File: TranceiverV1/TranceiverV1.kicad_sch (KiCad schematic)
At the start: 21 parts, among them J1 Conn_01x03_Socket, J3 Battery, J4 Conn_01x03_Pin, M1 Motor_Servo, SW1 SW_Push_Open, U1 NRF24L01_, U3 102010388, U4 LD1086DTTR

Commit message: changed switch
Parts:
- removed SW1: SW_Push_Open, Button_Switch_THT:SW_PUSH_1P1T_6x3.5mm_H5.0_APEM_MJTP1250, symbol Switch:SW_Push_Open
- added S3: ATE1D-2M3-10-Z, ATE1D-2M3-10-Z:SW_ATE1D-2M3-10-Z, symbol ATE1D-2M3-10-Z:ATE1D-2M3-10-Z
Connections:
- net GND: now also S3.3
- net Regulator_In: now also S3.1
- net at J3.1 (Pin_1): now also S3.2
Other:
- note added: "SW_SPST"
- moved on the sheet: J3

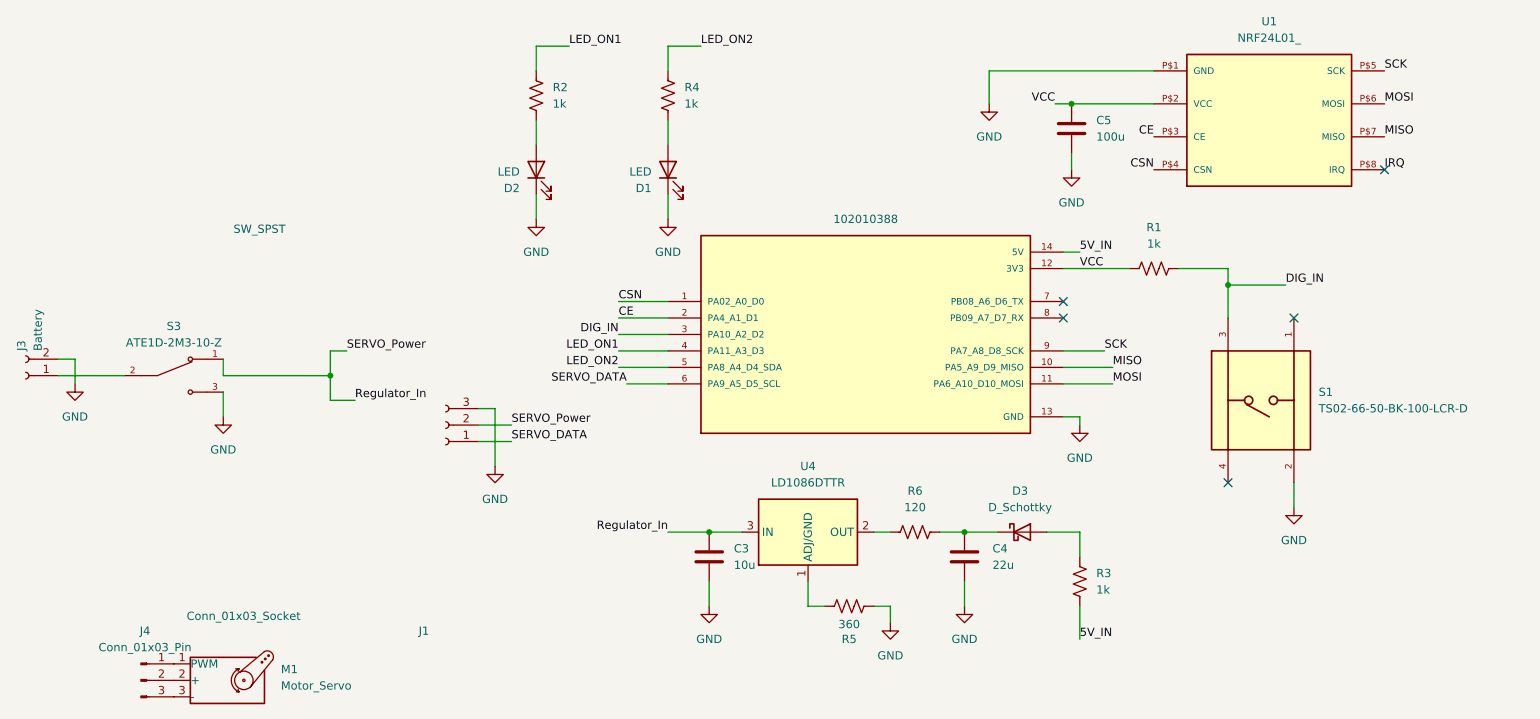
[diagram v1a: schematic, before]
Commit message: rewired traces and changed diode position added mounting holes
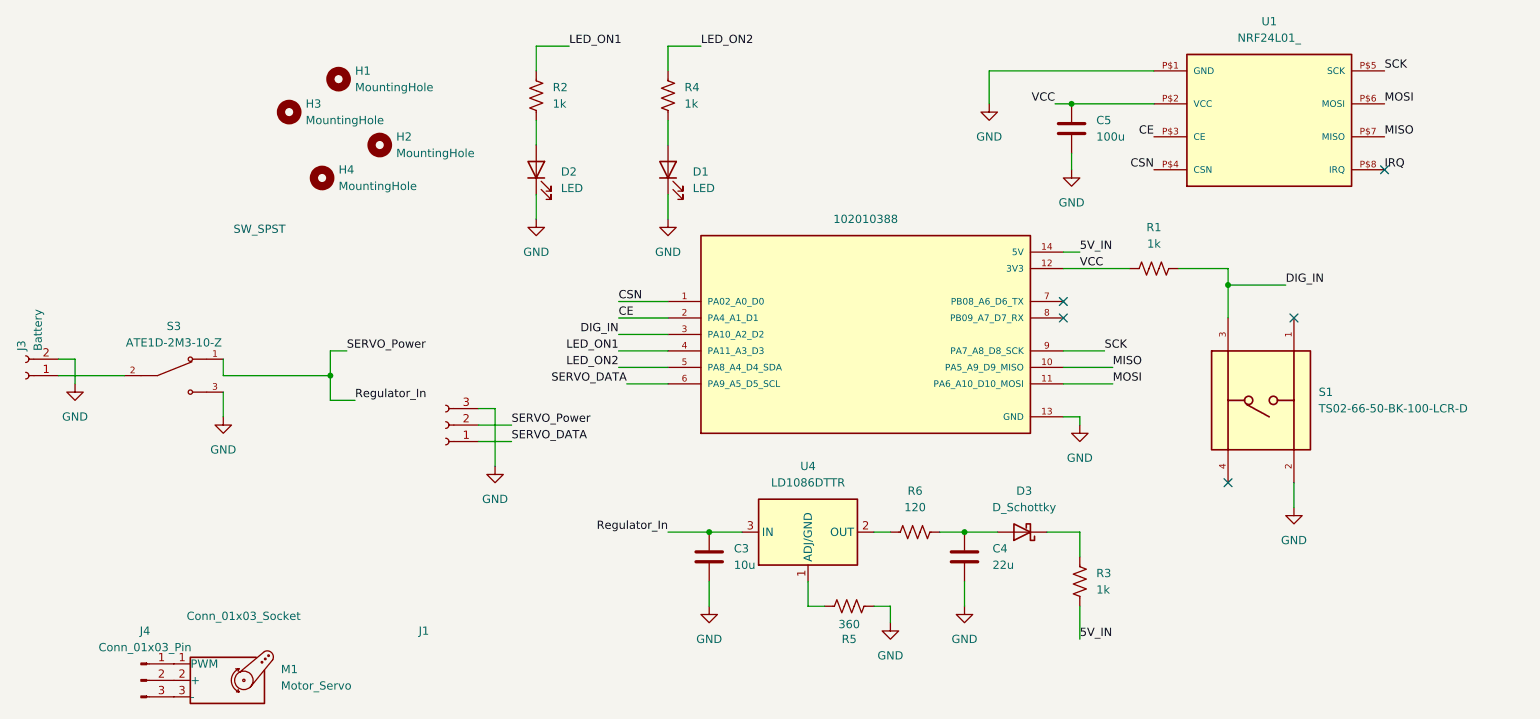
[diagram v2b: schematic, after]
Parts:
- added H1, H2, H3, H4: MountingHole, MountingHole:MountingHole_3.2mm_M3, symbol Mechanical:MountingHole
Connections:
- net at R3.1: now also D3.1 (K); no longer D3.2 (A)
- net at C4.1, R6.2: now also D3.2 (A); no longer D3.1 (K)
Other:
- moved on the sheet: D3
